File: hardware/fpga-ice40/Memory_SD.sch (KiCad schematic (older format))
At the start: 5 parts, among them J1 MicroSD_Molex_1040310811

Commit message: Reannotate schematic symbols
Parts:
- renumbered C30 to C16, C24 to C17, J1 to J2, R8 to R1
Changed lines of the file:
@@
 P 6000 5300
 AR Path="/5F8FA3AC" Ref="#PWR?"  Part="1"
-AR Path="/5F8F01DB/5F8FA3AC" Ref="#PWR0116"  Part="1"
-F 0 "#PWR0116" H 6000 5050 50  0001 C CNN
+AR Path="/5F8F01DB/5F8FA3AC" Ref="#PWR018"  Part="1"
+F 0 "#PWR018" H 6000 5050 50  0001 C CNN
 F 1 "GND" H 6003 5174 50  0000 C CNN
 F 2 "" H 5900 4950 50  0001 C CNN
@@
 P 6300 4500
 AR Path="/5F8FA3B4" Ref="J?"  Part="1"
-AR Path="/5F8F01DB/5F8FA3B4" Ref="J1"  Part="1"
-F 0 "J1" H 6250 5100 50  0000 L CNN
+AR Path="/5F8F01DB/5F8FA3B4" Ref="J2"  Part="1"
+F 0 "J2" H 6250 5100 50  0000 L CNN
 F 1 "MicroSD_Molex_1040310811" H 6250 5000 50  0000 L CNN
 F 2 "ng_conn:MicroSD_Molex_1040310811" H 6300 4500 50  0001 C CNN
@@
 P 5250 3650
 AR Path="/5F8FA3CB" Ref="R?"  Part="1"
-AR Path="/5F8F01DB/5F8FA3CB" Ref="R8"  Part="1"
-F 0 "R8" V 5300 3800 50  0000 L CNN
+AR Path="/5F8F01DB/5F8FA3CB" Ref="R1"  Part="1"
+F 0 "R1" V 5300 3800 50  0000 L CNN
 F 1 "10k" V 5300 3500 50  0000 R CNN
 F 2 "Resistor_SMD:R_0603_1608Metric" V 5180 3650 50  0001 C CNN
@@
 P 4600 3550
 AR Path="/5F8FA3E3" Ref="C?"  Part="1"
-AR Path="/5F8F01DB/5F8FA3E3" Ref="C30"  Part="1"
-F 0 "C30" H 4550 3650 50  0000 R CNN
+AR Path="/5F8F01DB/5F8FA3E3" Ref="C16"  Part="1"
+F 0 "C16" H 4550 3650 50  0000 R CNN
 F 1 "10u" H 4550 3450 50  0000 R CNN
 F 2 "Capacitor_SMD:C_0603_1608Metric" H 4638 3400 50  0001 C CNN
@@
 P 4900 3550
 AR Path="/5F8FA3E9" Ref="C?"  Part="1"
-AR Path="/5F8F01DB/5F8FA3E9" Ref="C24"  Part="1"
-F 0 "C24" H 4850 3650 50  0000 R CNN
+AR Path="/5F8F01DB/5F8FA3E9" Ref="C17"  Part="1"
+F 0 "C17" H 4850 3650 50  0000 R CNN
 F 1 "100n" H 4850 3450 50  0000 R CNN
 F 2 "Capacitor_SMD:C_0603_1608Metric" H 4938 3400 50  0001 C CNN
@@
 P 4600 3800
 AR Path="/5F8FA3EF" Ref="#PWR?"  Part="1"
-AR Path="/5F8F01DB/5F8FA3EF" Ref="#PWR0117"  Part="1"
-F 0 "#PWR0117" H 4600 3550 50  0001 C CNN
+AR Path="/5F8F01DB/5F8FA3EF" Ref="#PWR016"  Part="1"
+F 0 "#PWR016" H 4600 3550 50  0001 C CNN
 F 1 "GND" H 4603 3674 50  0000 C CNN
 F 2 "" H 4500 3450 50  0001 C CNN
@@
 P 4900 3800
 AR Path="/5F8FA3F5" Ref="#PWR?"  Part="1"
-AR Path="/5F8F01DB/5F8FA3F5" Ref="#PWR0118"  Part="1"
-F 0 "#PWR0118" H 4900 3550 50  0001 C CNN
+AR Path="/5F8F01DB/5F8FA3F5" Ref="#PWR017"  Part="1"
+F 0 "#PWR017" H 4900 3550 50  0001 C CNN
 F 1 "GND" H 4903 3674 50  0000 C CNN
 F 2 "" H 4800 3450 50  0001 C CNN

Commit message: Component selection by MPN and routing cleanup
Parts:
- C16: footprint Capacitor_SMD:C_0603_1608Metric -> Capacitor_SMD:C_0805_2012Metric; MPN (none) -> CL21A106KAYNNNE
- C17: MPN (none) -> CL10B104KB8NNNC
- J2: MPN (none) -> 104031-0811
- RN3: MPN (none) -> YC164-JR-0710KL
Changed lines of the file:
@@
 F 2 "ng_conn:MicroSD_Molex_1040310811" H 6300 4500 50  0001 C CNN
 F 3 "~" H 6300 4500 50  0001 C CNN
+F 4 "104031-0811" H 6300 4500 50  0001 C CNN "MPN"
 	1    6300 4500
 	1    0    0    -1
@@
 F 2 "Resistor_SMD:R_Array_Convex_4x0603" V 5875 3650 50  0001 C CNN
 F 3 "~" H 5600 3650 50  0001 C CNN
+F 4 "YC164-JR-0710KL" H 5600 3650 50  0001 C CNN "MPN"
 	1    5600 3650
 	1    0    0    -1
@@
 F 0 "C16" H 4550 3650 50  0000 R CNN
 F 1 "10u" H 4550 3450 50  0000 R CNN
-F 2 "Capacitor_SMD:C_0603_1608Metric" H 4638 3400 50  0001 C CNN
+F 2 "Capacitor_SMD:C_0805_2012Metric" H 4638 3400 50  0001 C CNN
 F 3 "~" H 4600 3550 50  0001 C CNN
+F 4 "CL21A106KAYNNNE" H 4600 3550 50  0001 C CNN "MPN"
 	1    4600 3550
 	-1   0    0    -1
@@
 F 2 "Capacitor_SMD:C_0603_1608Metric" H 4938 3400 50  0001 C CNN
 F 3 "~" H 4900 3550 50  0001 C CNN
+F 4 "CL10B104KB8NNNC" H 4900 3550 50  0001 C CNN "MPN"
 	1    4900 3550
 	-1   0    0    -1

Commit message: Complete component selection by MPN
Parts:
- R1: MPN (none) -> RC0603FR-0710KL
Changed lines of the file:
@@
 F 2 "Resistor_SMD:R_0603_1608Metric" V 5180 3650 50  0001 C CNN
 F 3 "~" H 5250 3650 50  0001 C CNN
+F 4 "RC0603FR-0710KL" H 5250 3650 50  0001 C CNN "MPN"
 	1    5250 3650
 	1    0    0    -1

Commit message: Completed verification of all pins for all symbols
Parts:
- added R8: 10k, Resistor_SMD:R_0603_1608Metric, symbol Device:R
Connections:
- net GND: now also J2.10 (DET)
- net P3V3: now also R8.1
- net SD_CD renamed SD_DET
- net SD_DET: now also R8.2
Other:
- moved on the sheet: C16, C17
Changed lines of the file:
@@
 L ng_power:GND #PWR?
 U 1 1 5F8FA3AC
-P 6000 5300
+P 6000 5400
 AR Path="/5F8FA3AC" Ref="#PWR?"  Part="1"
 AR Path="/5F8F01DB/5F8FA3AC" Ref="#PWR018"  Part="1"
-F 0 "#PWR018" H 6000 5050 50  0001 C CNN
-F 1 "GND" H 6003 5174 50  0000 C CNN
-F 2 "" H 5900 4950 50  0001 C CNN
-F 3 "" H 6000 5300 50  0001 C CNN
-	1    6000 5300
-	1    0    0    -1
-$EndComp
-Wire Wire Line
-	6300 5200 6000 5200
-Wire Wire Line
-	6300 5100 6300 5200
+F 0 "#PWR018" H 6000 5150 50  0001 C CNN
+F 1 "GND" H 6003 5274 50  0000 C CNN
+F 2 "" H 5900 5050 50  0001 C CNN
+F 3 "" H 6000 5400 50  0001 C CNN
+	1    6000 5400
+	1    0    0    -1
+$EndComp
 $Comp
 L ng_conn:MicroSD_Molex_1040310811 J?
@@
 Wire Wire Line
 	6000 4600 6100 4600
-Connection ~ 6000 5200
-Wire Wire Line
-	6000 5200 6000 5300
-Wire Wire Line
-	6000 4600 6000 5200
 Wire Wire Line
 	5400 3300 5500 3300
@@
 	1    0    0    -1
 $EndComp
-Text GLabel 5150 4500 0    50   Input ~ 0
+Text GLabel 4950 4500 0    50   Input ~ 0
 SD_CLK
-Text GLabel 5150 4700 0    50   Input ~ 0
+Text GLabel 4950 4700 0    50   Input ~ 0
 SD_DAT0
-Text GLabel 5150 4800 0    50   Input ~ 0
+Text GLabel 4950 4800 0    50   Input ~ 0
 SD_DAT1
-Text GLabel 5150 4300 0    50   Input ~ 0
+Text GLabel 4950 4300 0    50   Input ~ 0
 SD_CMD
-Text GLabel 5150 4200 0    50   Input ~ 0
+Text GLabel 4950 4200 0    50   Input ~ 0
 SD_DAT3
-Text GLabel 5150 4100 0    50   Input ~ 0
+Text GLabel 4950 4100 0    50   Input ~ 0
 SD_DAT2
 $Comp
@@
 $EndComp
 Wire Wire Line
-	6100 4500 5150 4500
+	6100 4500 4950 4500
 Wire Wire Line
 	6100 4400 6000 4400
@@
 Connection ~ 5700 3300
 Wire Wire Line
-	4900 3400 4900 3300
-Wire Wire Line
-	4600 3300 4600 3400
+	4800 3400 4800 3300
+Wire Wire Line
+	4500 3300 4500 3400
 $Comp
 L Device:C C?
 U 1 1 5F8FA3E3
-P 4600 3550
+P 4500 3550
 AR Path="/5F8FA3E3" Ref="C?"  Part="1"
 AR Path="/5F8F01DB/5F8FA3E3" Ref="C16"  Part="1"
-F 0 "C16" H 4550 3650 50  0000 R CNN
-F 1 "10u" H 4550 3450 50  0000 R CNN
-F 2 "Capacitor_SMD:C_0805_2012Metric" H 4638 3400 50  0001 C CNN
-F 3 "~" H 4600 3550 50  0001 C CNN
-F 4 "CL21A106KAYNNNE" H 4600 3550 50  0001 C CNN "MPN"
-	1    4600 3550
+F 0 "C16" H 4450 3650 50  0000 R CNN
+F 1 "10u" H 4450 3450 50  0000 R CNN
+F 2 "Capacitor_SMD:C_0805_2012Metric" H 4538 3400 50  0001 C CNN
+F 3 "~" H 4500 3550 50  0001 C CNN
+F 4 "CL21A106KAYNNNE" H 4500 3550 50  0001 C CNN "MPN"
+	1    4500 3550
 	-1   0    0    -1
 $EndComp
@@
 L Device:C C?
 U 1 1 5F8FA3E9
-P 4900 3550
+P 4800 3550
 AR Path="/5F8FA3E9" Ref="C?"  Part="1"
 AR Path="/5F8F01DB/5F8FA3E9" Ref="C17"  Part="1"
-F 0 "C17" H 4850 3650 50  0000 R CNN
-F 1 "100n" H 4850 3450 50  0000 R CNN
-F 2 "Capacitor_SMD:C_0603_1608Metric" H 4938 3400 50  0001 C CNN
-F 3 "~" H 4900 3550 50  0001 C CNN
-F 4 "CL10B104KB8NNNC" H 4900 3550 50  0001 C CNN "MPN"
-	1    4900 3550
+F 0 "C17" H 4750 3650 50  0000 R CNN
+F 1 "100n" H 4750 3450 50  0000 R CNN
+F 2 "Capacitor_SMD:C_0603_1608Metric" H 4838 3400 50  0001 C CNN
+F 3 "~" H 4800 3550 50  0001 C CNN
+F 4 "CL10B104KB8NNNC" H 4800 3550 50  0001 C CNN "MPN"
+	1    4800 3550
 	-1   0    0    -1
 $EndComp
@@
 L ng_power:GND #PWR?
 U 1 1 5F8FA3EF
-P 4600 3800
+P 4500 3800
 AR Path="/5F8FA3EF" Ref="#PWR?"  Part="1"
 AR Path="/5F8F01DB/5F8FA3EF" Ref="#PWR016"  Part="1"
-F 0 "#PWR016" H 4600 3550 50  0001 C CNN
-F 1 "GND" H 4603 3674 50  0000 C CNN
-F 2 "" H 4500 3450 50  0001 C CNN
-F 3 "" H 4600 3800 50  0001 C CNN
-	1    4600 3800
+F 0 "#PWR016" H 4500 3550 50  0001 C CNN
+F 1 "GND" H 4503 3674 50  0000 C CNN
+F 2 "" H 4400 3450 50  0001 C CNN
+F 3 "" H 4500 3800 50  0001 C CNN
+	1    4500 3800
 	1    0    0    -1
 $EndComp
@@
 L ng_power:GND #PWR?
 U 1 1 5F8FA3F5
-P 4900 3800
+P 4800 3800
 AR Path="/5F8FA3F5" Ref="#PWR?"  Part="1"
 AR Path="/5F8F01DB/5F8FA3F5" Ref="#PWR017"  Part="1"
-F 0 "#PWR017" H 4900 3550 50  0001 C CNN
-F 1 "GND" H 4903 3674 50  0000 C CNN
-F 2 "" H 4800 3450 50  0001 C CNN
-F 3 "" H 4900 3800 50  0001 C CNN
-	1    4900 3800
-	1    0    0    -1
-$EndComp
-Wire Wire Line
-	4900 3700 4900 3800
-Wire Wire Line
-	4900 3300 4600 3300
-Text GLabel 4500 3300 0    50   UnSpc ~ 0
+F 0 "#PWR017" H 4800 3550 50  0001 C CNN
+F 1 "GND" H 4803 3674 50  0000 C CNN
+F 2 "" H 4700 3450 50  0001 C CNN
+F 3 "" H 4800 3800 50  0001 C CNN
+	1    4800 3800
+	1    0    0    -1
+$EndComp
+Wire Wire Line
+	4800 3700 4800 3800
+Wire Wire Line
+	4800 3300 4500 3300
+Text GLabel 4400 3300 0    50   UnSpc ~ 0
 P3V3
 Wire Wire Line
-	5150 4100 5250 4100
-Wire Wire Line
-	4900 3300 5250 3300
-Connection ~ 4900 3300
-Connection ~ 5250 3300
+	4950 4100 5250 4100
+Wire Wire Line
+	4800 3300 5150 3300
+Connection ~ 4800 3300
 Connection ~ 5250 4100
 Wire Wire Line
@@
 	6000 3300 6000 4400
 Wire Wire Line
-	4600 3700 4600 3800
-Connection ~ 4600 3300
-Wire Wire Line
-	4600 3300 4500 3300
-Wire Wire Line
-	5150 4700 5500 4700
-Wire Wire Line
-	5150 4300 5600 4300
+	4500 3700 4500 3800
+Connection ~ 4500 3300
+Wire Wire Line
+	4500 3300 4400 3300
+Wire Wire Line
+	4950 4700 5500 4700
+Wire Wire Line
+	4950 4300 5600 4300
 Wire Wire Line
 	5500 3850 5500 4700
@@
 	5600 4300 6100 4300
 Wire Wire Line
-	5150 4200 5700 4200
-Wire Wire Line
-	5150 4800 5400 4800
+	4950 4200 5700 4200
+Wire Wire Line
+	4950 4800 5400 4800
 Wire Wire Line
 	5700 3850 5700 4200
@@
 Wire Wire Line
 	5400 4800 6100 4800
-Text GLabel 5150 4900 0    50   Input ~ 0
-SD_CD
+Text GLabel 4950 4900 0    50   Input ~ 0
+SD_DET
+Wire Wire Line
+	4950 4900 5150 4900
+Connection ~ 5250 3300
+Wire Wire Line
+	5150 3500 5150 3300
+$Comp
+L Device:R R?
+U 1 1 5EFEABF6
+P 5150 3650
+AR Path="/5EFEABF6" Ref="R?"  Part="1"
+AR Path="/5F8F01DB/5EFEABF6" Ref="R8"  Part="1"
+F 0 "R8" V 5200 3800 50  0000 L CNN
+F 1 "10k" V 5200 3500 50  0000 R CNN
+F 2 "Resistor_SMD:R_0603_1608Metric" V 5080 3650 50  0001 C CNN
+F 3 "~" H 5150 3650 50  0001 C CNN
+F 4 "RC0603FR-0710KL" H 5150 3650 50  0001 C CNN "MPN"
+	1    5150 3650
+	1    0    0    -1
+$EndComp
+Connection ~ 5150 3300
+Wire Wire Line
+	5150 3300 5250 3300
+Wire Wire Line
+	5150 3800 5150 4900
+Connection ~ 5150 4900
 Wire Wire Line
 	5150 4900 6100 4900
+Wire Wire Line
+	6000 4600 6000 5000
+Wire Wire Line
+	6100 5000 6000 5000
+Connection ~ 6000 5000
+Wire Wire Line
+	6000 5000 6000 5300
+Wire Wire Line
+	6300 5200 6300 5300
+Wire Wire Line
+	6300 5300 6000 5300
+Connection ~ 6000 5300
+Wire Wire Line
+	6000 5300 6000 5400
 $EndSCHEMATC

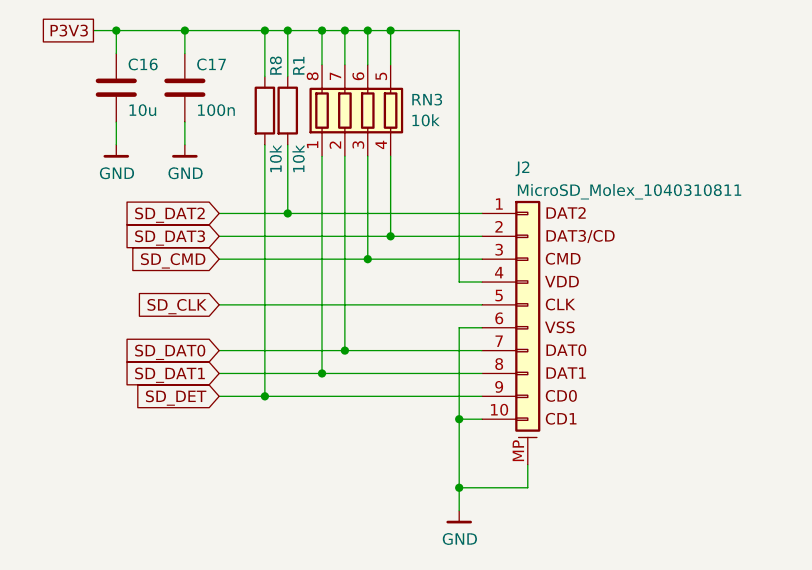
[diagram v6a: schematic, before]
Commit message: Rename SD_DET signal to SD_CD for consistency
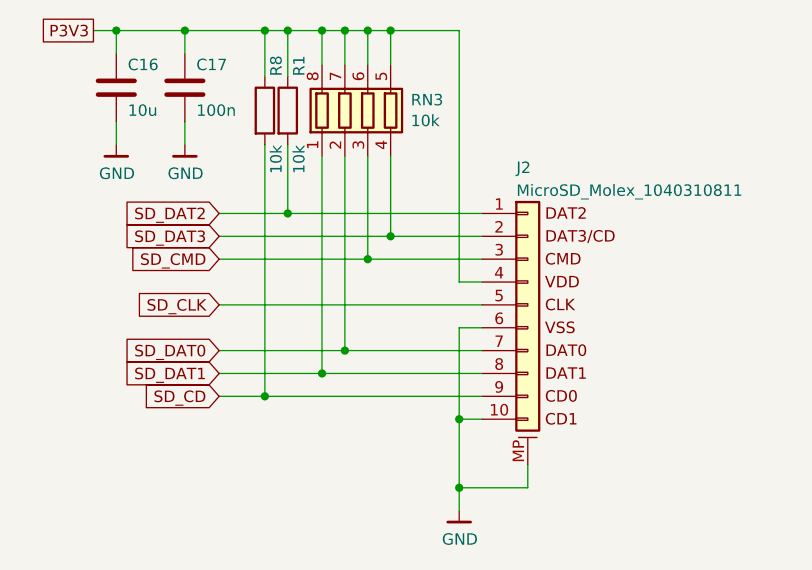
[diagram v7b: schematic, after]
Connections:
- net SD_DET renamed SD_CD
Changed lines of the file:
@@
 	5400 4800 6100 4800
 Text GLabel 4950 4900 0    50   Input ~ 0
-SD_DET
+SD_CD
 Wire Wire Line
 	4950 4900 5150 4900

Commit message: Fix mechanical issue by moving USB connector to top of board
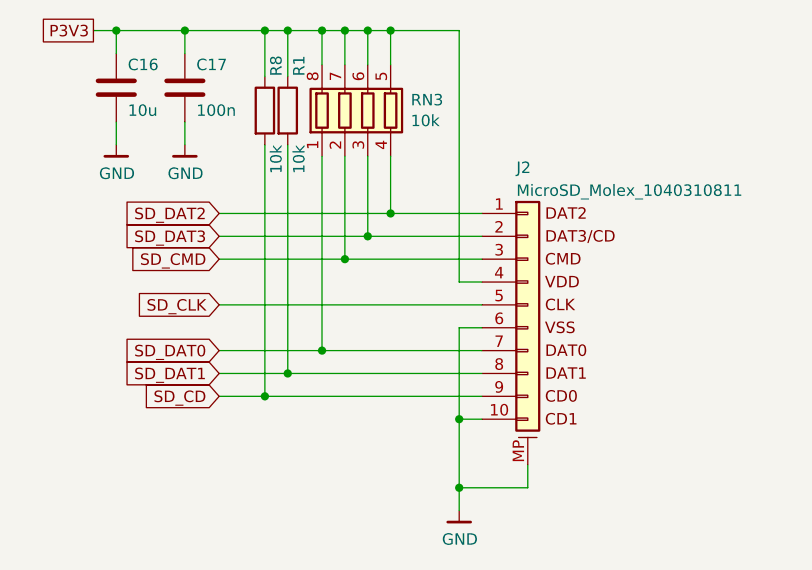
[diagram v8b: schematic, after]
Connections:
- net SD_CMD: now also RN3.2 (R2.1); no longer RN3.3 (R3.1)
- net SD_DAT0: now also RN3.1 (R1.1); no longer RN3.2 (R2.1)
- net SD_DAT1: now also R1.2; no longer RN3.1 (R1.1)
- net SD_DAT2: now also RN3.4 (R4.1); no longer R1.2
- net SD_DAT3: now also RN3.3 (R3.1); no longer RN3.4 (R4.1)
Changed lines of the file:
@@
 Wire Wire Line
 	5250 3500 5250 3300
-Wire Wire Line
-	5250 4100 5250 3800
 $Comp
 L Device:R R?
@@
 P3V3
 Wire Wire Line
-	4950 4100 5250 4100
-Wire Wire Line
 	4800 3300 5150 3300
 Connection ~ 4800 3300
-Connection ~ 5250 4100
-Wire Wire Line
-	5250 4100 6100 4100
 Wire Wire Line
 	6000 3300 6000 4400
@@
 	4500 3300 4400 3300
 Wire Wire Line
-	4950 4700 5500 4700
-Wire Wire Line
-	4950 4300 5600 4300
-Wire Wire Line
-	5500 3850 5500 4700
-Connection ~ 5500 4700
-Wire Wire Line
-	5500 4700 6100 4700
-Wire Wire Line
-	5600 3850 5600 4300
-Connection ~ 5600 4300
-Wire Wire Line
-	5600 4300 6100 4300
-Wire Wire Line
-	4950 4200 5700 4200
-Wire Wire Line
-	4950 4800 5400 4800
-Wire Wire Line
-	5700 3850 5700 4200
-Connection ~ 5700 4200
-Wire Wire Line
-	5700 4200 6100 4200
-Wire Wire Line
-	5400 3850 5400 4800
-Connection ~ 5400 4800
-Wire Wire Line
-	5400 4800 6100 4800
+	4950 4700 5400 4700
+Wire Wire Line
+	4950 4300 5500 4300
+Wire Wire Line
+	4950 4200 5600 4200
+Wire Wire Line
+	4950 4800 5250 4800
 Text GLabel 4950 4900 0    50   Input ~ 0
 SD_CD
@@
 Wire Wire Line
 	6000 5300 6000 5400
+Wire Wire Line
+	4950 4100 5700 4100
+Wire Wire Line
+	5250 3800 5250 4800
+Connection ~ 5250 4800
+Wire Wire Line
+	5250 4800 6100 4800
+Wire Wire Line
+	5400 4700 5400 3850
+Connection ~ 5400 4700
+Wire Wire Line
+	5400 4700 6100 4700
+Wire Wire Line
+	5500 4300 5500 3850
+Connection ~ 5500 4300
+Wire Wire Line
+	5500 4300 6100 4300
+Wire Wire Line
+	5600 4200 5600 3850
+Connection ~ 5600 4200
+Wire Wire Line
+	5600 4200 6100 4200
+Wire Wire Line
+	5700 4100 5700 3850
+Connection ~ 5700 4100
+Wire Wire Line
+	5700 4100 6100 4100
 $EndSCHEMATC
